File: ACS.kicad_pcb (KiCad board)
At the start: 2 copper layers, 30 parts, among them J1 5v? Igniter power source, J2 RJ45, J3 RJ45, P1 CONN_01X02, P10 ABT TOG, P11 LOX MPV, P12 LNCH SFT, P13 LNCH TOG, P14 CH4 MPV, P15 LOX VNT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

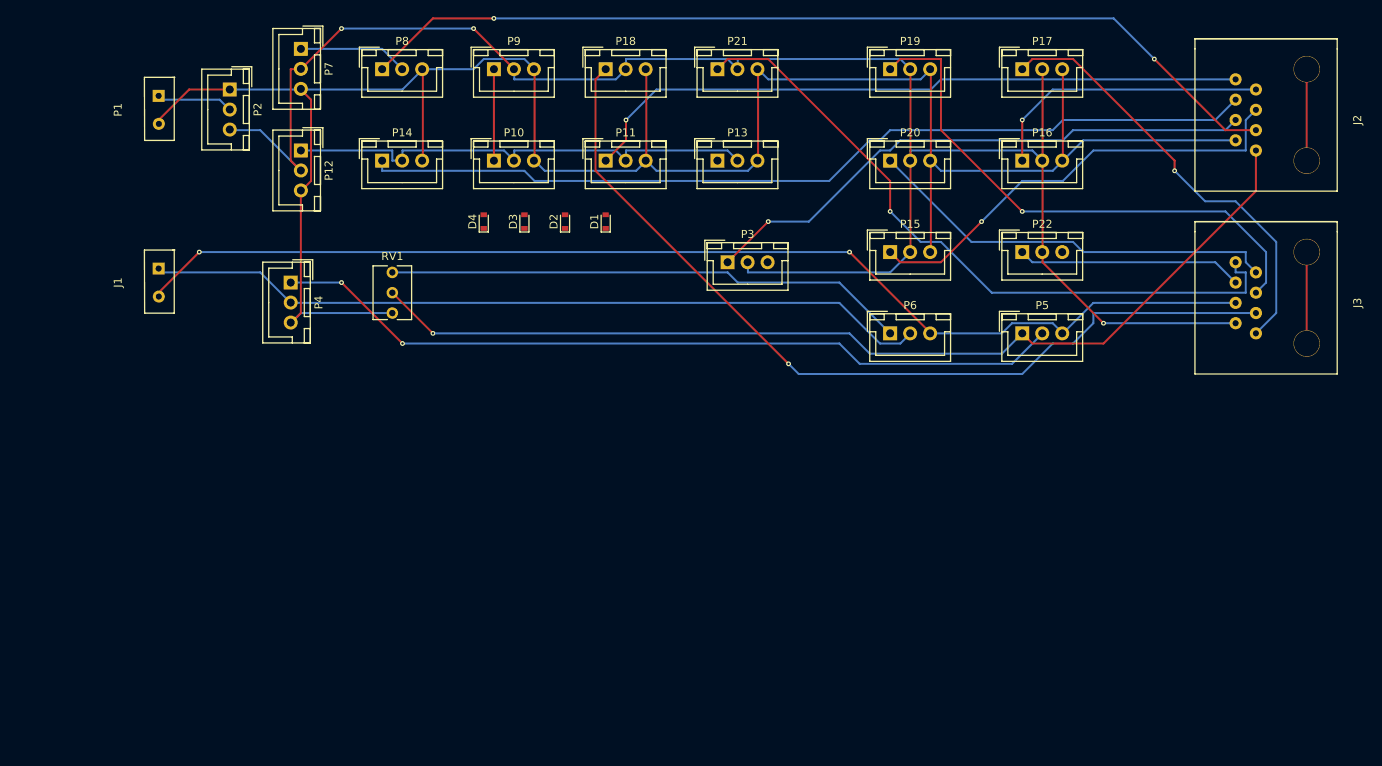
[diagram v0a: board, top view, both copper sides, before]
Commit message: Finished traces, and edge border
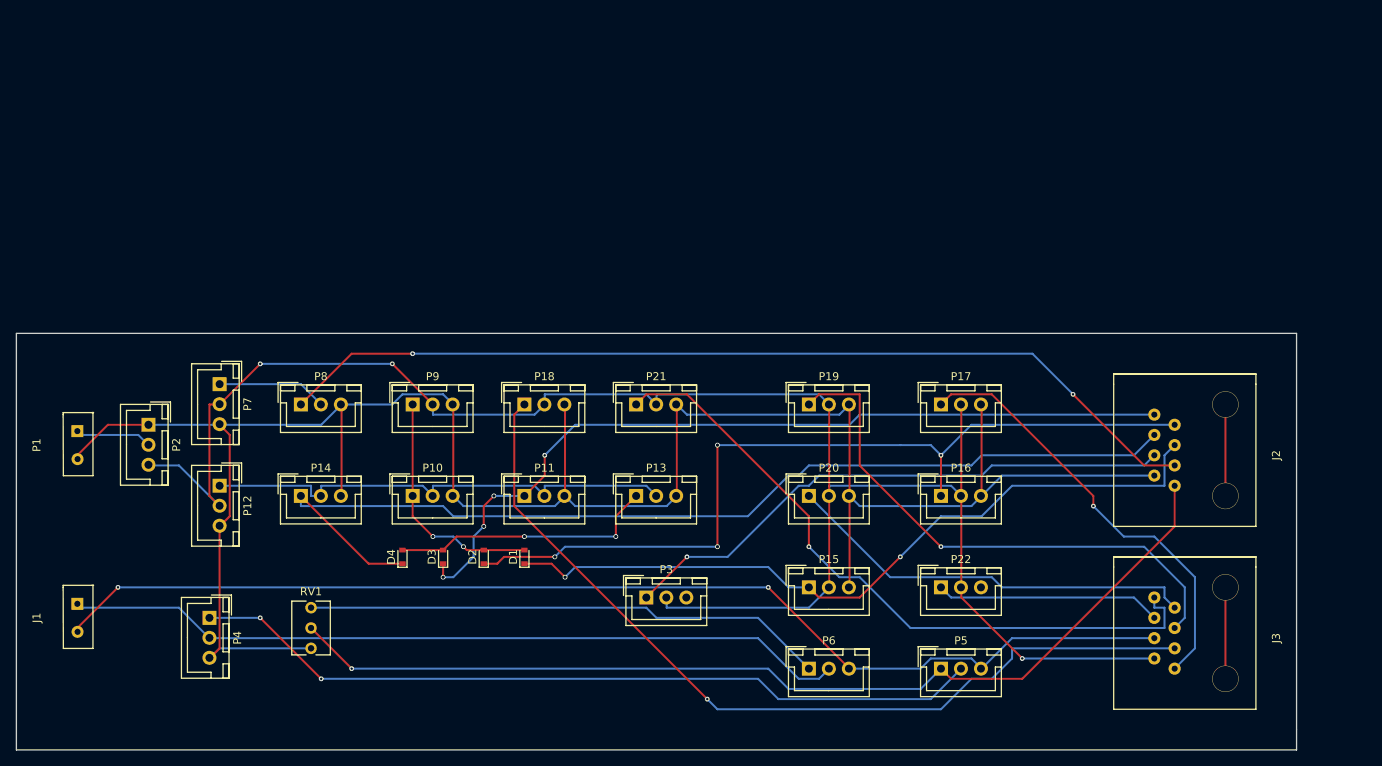
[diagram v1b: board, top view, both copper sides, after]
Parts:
- moved P18 43.1 mm to (121.9, 67.3)
- moved P21 43.1 mm to (135.9, 67.3)
- moved D1 43.1 mm to (121.9, 86.4)
- moved D2 43.1 mm to (116.8, 86.4)
- moved D3 43.1 mm to (111.8, 86.4)
- moved D4 43.1 mm to (106.7, 86.4)
- moved J1 43.1 mm to (66.0, 94.0)
- moved J2 43.1 mm to (201.9, 72.4)
- moved J3 43.1 mm to (201.9, 95.2)
- moved P1 43.1 mm to (66.0, 72.4)
- moved P10 43.1 mm to (108.0, 78.7)
- moved P11 43.1 mm to (121.9, 78.7)
- moved P12 43.1 mm to (83.8, 77.5)
- moved P13 43.1 mm to (135.9, 78.7)
- moved P14 43.1 mm to (94.0, 78.7)
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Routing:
- net Net-(D2-Pad1): track 35.9 -> 107.1 mm, vias 1 -> 4
- net Net-(D1-Pad1): track 56.4 -> 94.2 mm, vias 1 -> 2
- net Net-(D3-Pad2): track 0.00 -> 33.5 mm, vias 0 -> 2
- net Net-(D3-Pad1): track 84.4 -> 103.5 mm, vias 1 -> 4
- net Net-(D1-Pad2): track 11.4 -> 29.7 mm, vias 0 -> 2
- net Net-(D4-Pad1): track 112.7 -> 128.9 mm
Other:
- board outline added: 160 x 52.1 mm
